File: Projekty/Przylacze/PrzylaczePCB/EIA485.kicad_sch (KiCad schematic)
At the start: 33 parts, among them Q10 BC557, Q11 BC547, Q12 BC547, Q9 2N7002, U4 MAX3485, U5 MAX3485

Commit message: Przyłącze - schemat elektryczny v1.1
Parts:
- D3, D5: footprint (none) -> 1_WLASNA_Library:2PAD_WIRE
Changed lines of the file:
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@@
       (effects (font (size 1.27 1.27)) (justify right))
     )
-    (property "Footprint" "" (at 130.81 130.81 0)
+    (property "Footprint" "1_WLASNA_Library:2PAD_WIRE" (at 130.81 130.81 0)
       (effects (font (size 1.27 1.27)) hide)
     )
@@
       (effects (font (size 1.27 1.27)) (justify right))
     )
-    (property "Footprint" "" (at 86.36 129.54 0)
-      (effects (font (size 1.27 1.27)) hide)
-    )
+    (property "Footprint" "1_WLASNA_Library:2PAD_WIRE" (at 86.36 129.54 0)
+      (effects (font (size 1.27 1.27)) hide)
+    )

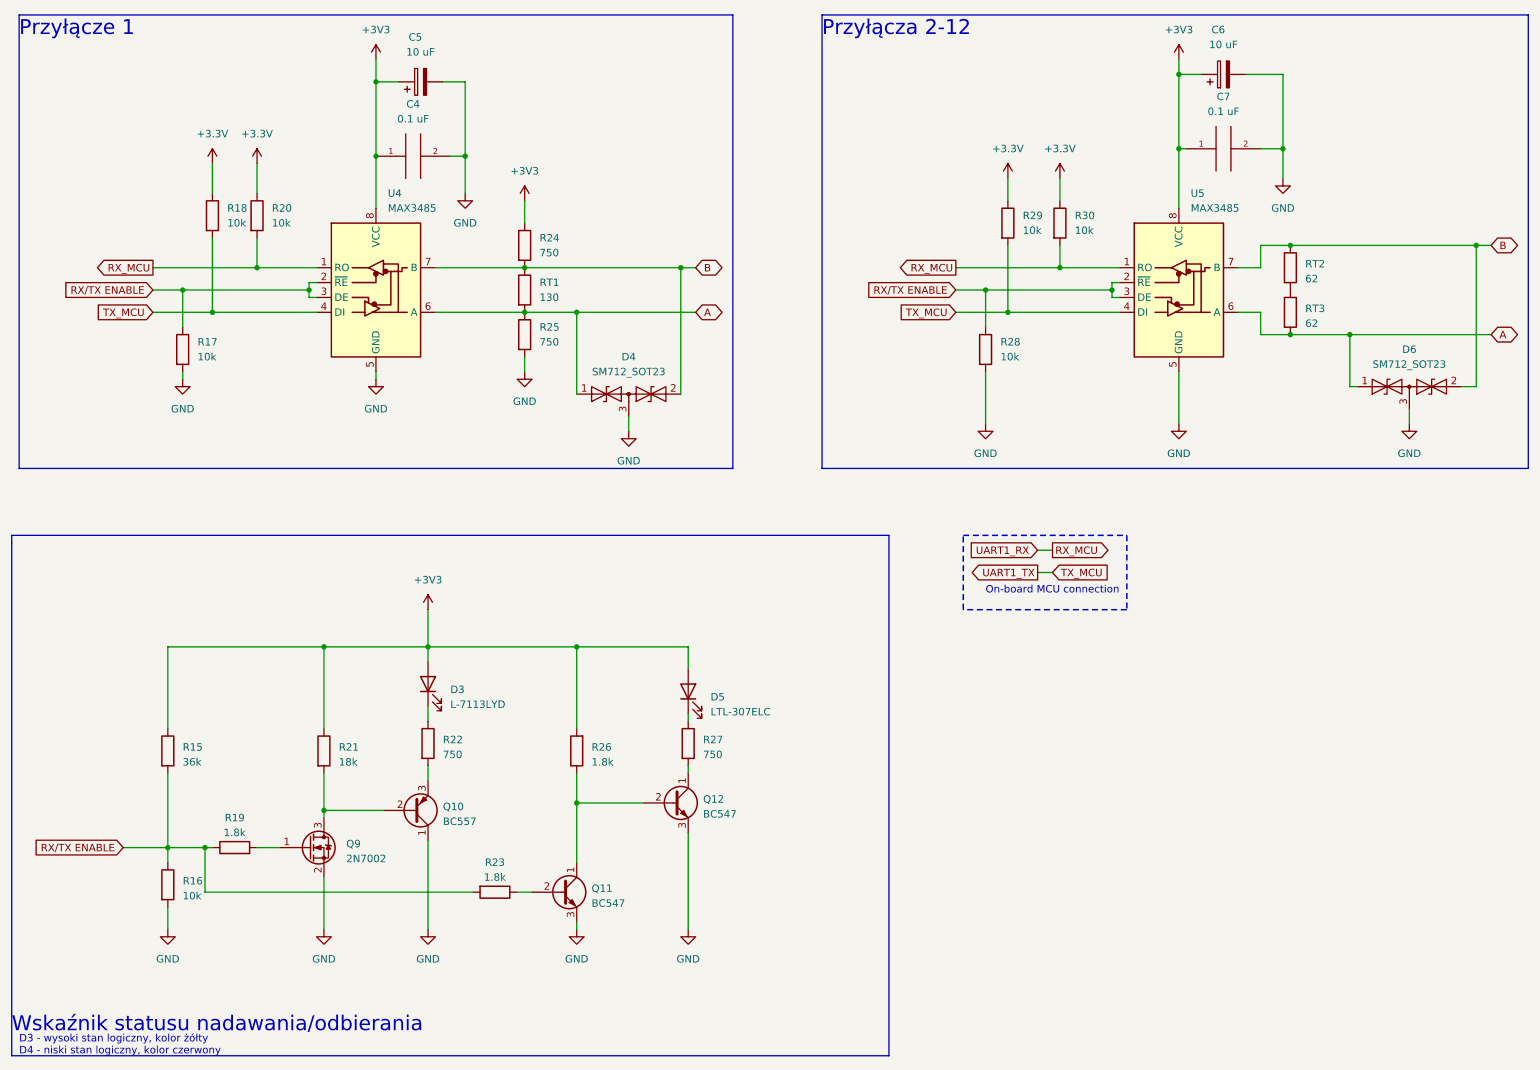
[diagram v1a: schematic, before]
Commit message: Połączenie w jeden schemat przyłącza sieci EIA485
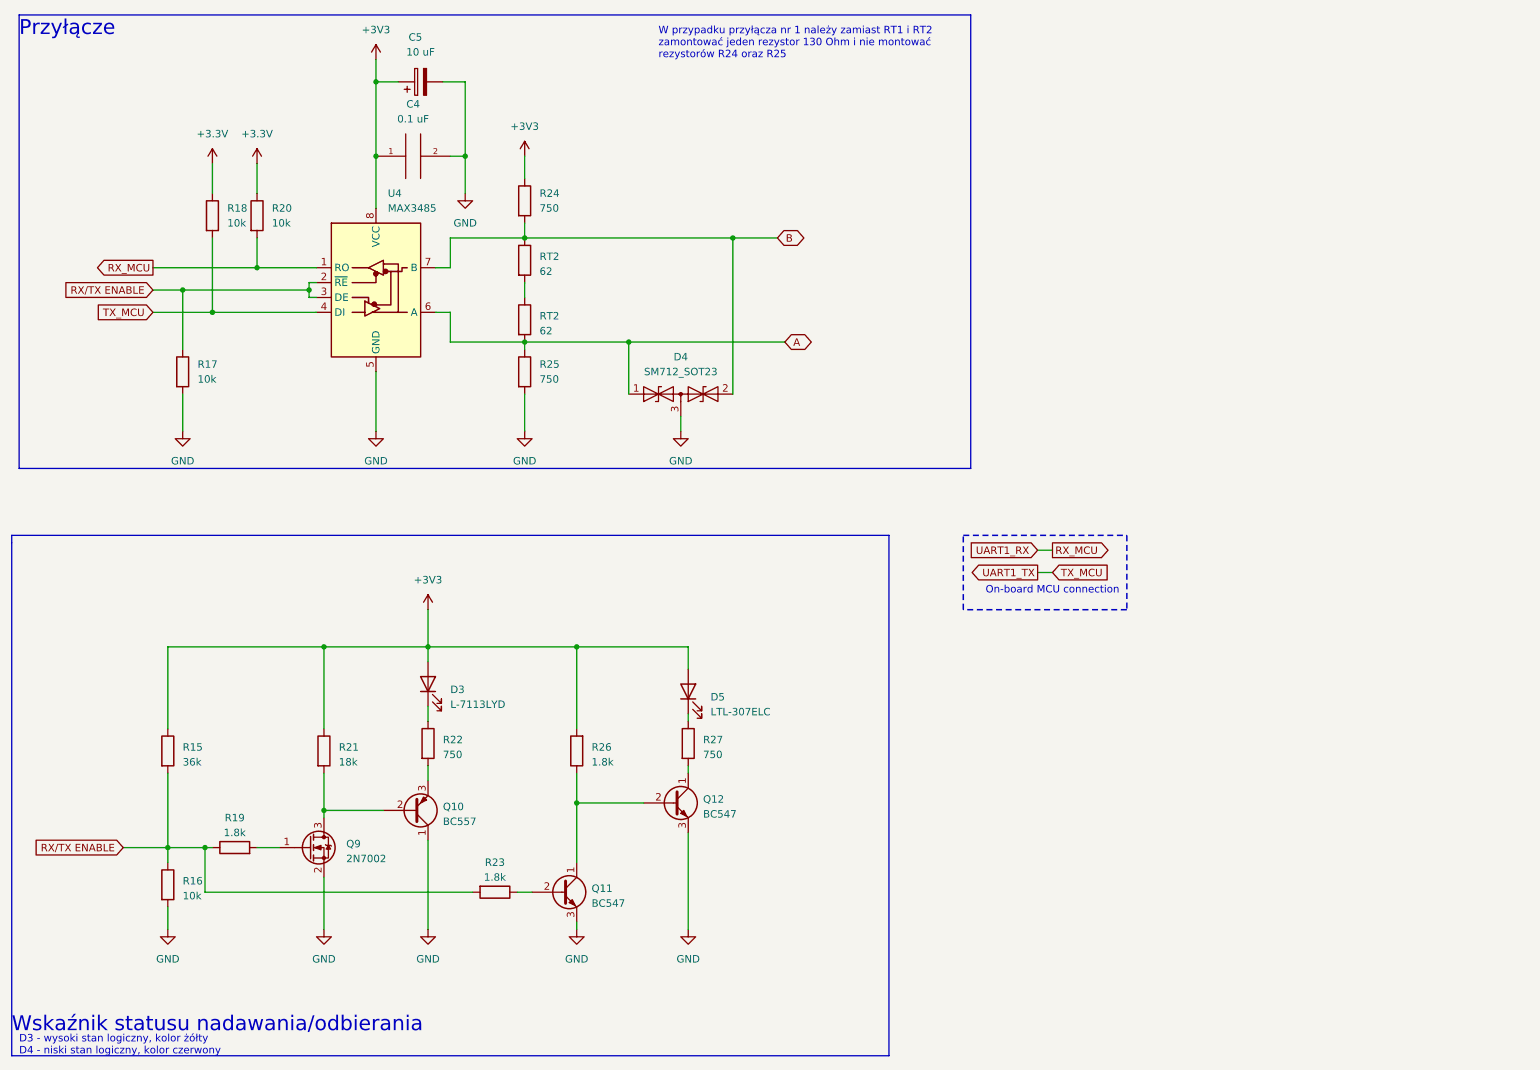
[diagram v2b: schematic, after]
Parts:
- removed C6: 10 uF, Capacitor_THT:CP_Radial_Tantal_D10.5mm_P5.00mm, symbol Device:C_Polarized
- removed C7: 0.1 uF, Capacitor_THT:C_Disc_D3.0mm_W1.6mm_P2.50mm, symbol pspice:C
- removed D6: SM712_SOT23, Package_TO_SOT_SMD:SOT-23, symbol Diode:SM712_SOT23
- removed R28, R29, R30: 10k, Resistor_THT:R_Axial_DIN0207_L6.3mm_D2.5mm_P7.62mm_Horizontal, symbol Device:R
- removed RT1: 130, Resistor_THT:R_Axial_DIN0207_L6.3mm_D2.5mm_P5.08mm_Vertical, symbol Device:R
- removed RT2, RT3: 62, Resistor_THT:R_Axial_DIN0207_L6.3mm_D2.5mm_P7.62mm_Horizontal, symbol Device:R
- removed U5: MAX3485, Package_SO:SO-8_3.9x4.9mm_P1.27mm, symbol Interface_UART:MAX3485
- added RT2 (x2): 62, Resistor_THT:R_Axial_DIN0207_L6.3mm_D2.5mm_P7.62mm_Horizontal, symbol Device:R
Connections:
- net A: now also RT2.2
- net B: now also RT2.1
- new net: RT2.1, RT2.2
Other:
- note added: "Przyłącze"
- note added: "W przypadku przyłącza nr 1 należy zamiast RT1 i RT2 zamontować jeden rezystor 130 Ohm i nie montować rezystorów R24 oraz R25"
- note removed: "Przyłącza 2-12"
- note removed: "Przyłącze 1"
- moved on the sheet: D4, R17, R24, R25

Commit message: Przyłącze - schemat elektryczny v1.2
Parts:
- C4: symbol pspice:C -> Device:C
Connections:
- net +3V3 renamed +3.3V
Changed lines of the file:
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@@
 (kicad_sch (version 20230121) (generator eeschema)
   (paper "A4")
+  (junction (at 66.04 62.23) (diameter 0) (color 0 0 0 0)
+  )
+  (junction (at 77.47 26.67) (diameter 0) (color 0 0 0 0)
+  )
+  (junction (at 111.76 149.86) (diameter 0) (color 0 0 0 0)
+  )
+  (junction (at 92.71 39.37) (diameter 0) (color 0 0 0 0)
+  )
+  (junction (at 102.87 71.12) (diameter 0) (color 0 0 0 0)
+  )
+  (junction (at 138.43 53.34) (diameter 0) (color 0 0 0 0)
+  )
+  (junction (at 68.58 123.19) (diameter 0) (color 0 0 0 0)
+  )
+  (junction (at 86.36 123.19) (diameter 0) (color 0 0 0 0)
+  )
+  (junction (at 120.65 71.12) (diameter 0) (color 0 0 0 0)
+  )
+  (junction (at 41.91 157.48) (diameter 0) (color 0 0 0 0)
+  )
+  (junction (at 57.15 58.42) (diameter 0) (color 0 0 0 0)
+  )
+  (junction (at 44.45 62.23) (diameter 0) (color 0 0 0 0)
+  )
+  (junction (at 68.58 151.13) (diameter 0) (color 0 0 0 0)
+  )
+  (junction (at 102.87 53.34) (diameter 0) (color 0 0 0 0)
+  )
+  (junction (at 49.53 66.04) (diameter 0) (color 0 0 0 0)
+  )
   (junction (at 77.47 39.37) (diameter 0) (color 0 0 0 0)
   )
-  (junction (at 66.04 62.23) (diameter 0) (color 0 0 0 0)
-  )
-  (junction (at 77.47 26.67) (diameter 0) (color 0 0 0 0)
-  )
-  (junction (at 111.76 149.86) (diameter 0) (color 0 0 0 0)
-  )
-  (junction (at 92.71 39.37) (diameter 0) (color 0 0 0 0)
-  )
-  (junction (at 102.87 71.12) (diameter 0) (color 0 0 0 0)
-  )
-  (junction (at 138.43 53.34) (diameter 0) (color 0 0 0 0)
-  )
-  (junction (at 68.58 123.19) (diameter 0) (color 0 0 0 0)
-  )
-  (junction (at 86.36 123.19) (diameter 0) (color 0 0 0 0)
-  )
-  (junction (at 120.65 71.12) (diameter 0) (color 0 0 0 0)
-  )
-  (junction (at 41.91 157.48) (diameter 0) (color 0 0 0 0)
-  )
-  (junction (at 57.15 58.42) (diameter 0) (color 0 0 0 0)
-  )
-  (junction (at 44.45 62.23) (diameter 0) (color 0 0 0 0)
-  )
-  (junction (at 68.58 151.13) (diameter 0) (color 0 0 0 0)
-  )
-  (junction (at 102.87 53.34) (diameter 0) (color 0 0 0 0)
-  )
-  (junction (at 49.53 66.04) (diameter 0) (color 0 0 0 0)
-  )
   (junction (at 111.76 123.19) (diameter 0) (color 0 0 0 0)
   )
@@
     (stroke (width 0) (type default))
   )
-  (wire (pts (xy 90.17 39.37) (xy 92.71 39.37))
+  (wire (pts (xy 87.63 39.37) (xy 92.71 39.37))
     (stroke (width 0) (type default))
   )
@@
   )
   (wire (pts (xy 57.15 40.64) (xy 57.15 45.72))
+    (stroke (width 0) (type default))
+  )
+  (wire (pts (xy 77.47 39.37) (xy 80.01 39.37))
     (stroke (width 0) (type default))
   )
@@
     )
   )
-  (symbol (lib_id "power:+3V3") (at 77.47 22.86 0) (unit 1)
-    (in_bom yes) (on_board yes) (dnp no) (fields_autoplaced)
-    (property "Reference" "#PWR024" (at 77.47 26.67 0)
-      (effects (font (size 1.27 1.27)) hide)
-    )
-    (property "Value" "+3V3" (at 77.47 17.78 0)
-      (effects (font (size 1.27 1.27)))
-    )
-    (property "Footprint" "" (at 77.47 22.86 0)
-      (effects (font (size 1.27 1.27)) hide)
-    )
-    (property "Datasheet" "" (at 77.47 22.86 0)
-      (effects (font (size 1.27 1.27)) hide)
-    )
-    (pin "1")
-    (instances
-      (project "PrzylaczePCB"
-        (path "/45db4533-aa6e-4785-aef0-204976ca4e66"
-          (reference "#PWR024") (unit 1)
-        )
-        (path "/45db4533-aa6e-4785-aef0-204976ca4e66/ce7112af-9253-43da-ac3f-57b598b98707"
-          (reference "#PWR027") (unit 1)
-        )
-      )
-      (project "rs485-przylacze"
-        (path "/84d4e166-b429-409a-ab37-c6a10fd82ff5"
-          (reference "#PWR?") (unit 1)
+  (symbol (lib_id "power:+3.3V") (at 86.36 116.84 0) (unit 1)
+    (in_bom yes) (on_board yes) (dnp no)
+    (property "Reference" "#PWR014" (at 86.36 120.65 0)
+      (effects (font (size 1.27 1.27)) hide)
+    )
+    (property "Value" "+3.3V" (at 86.36 113.03 0)
+      (effects (font (size 1.27 1.27)))
+    )
+    (property "Footprint" "" (at 86.36 116.84 0)
+      (effects (font (size 1.27 1.27)) hide)
+    )
+    (property "Datasheet" "" (at 86.36 116.84 0)
+      (effects (font (size 1.27 1.27)) hide)
+    )
+    (pin "1")
+    (instances
+      (project "PrzylaczePCB"
+        (path "/45db4533-aa6e-4785-aef0-204976ca4e66"
+          (reference "#PWR014") (unit 1)
+        )
+        (path "/45db4533-aa6e-4785-aef0-204976ca4e66/ce7112af-9253-43da-ac3f-57b598b98707"
+          (reference "#PWR019") (unit 1)
         )
       )
@@
     )
   )
-  (symbol (lib_id "pspice:C") (at 83.82 39.37 90) (unit 1)
+  (symbol (lib_id "Device:C") (at 83.82 39.37 90) (unit 1)
     (in_bom yes) (on_board yes) (dnp no) (fields_autoplaced)
     (property "Reference" "C4" (at 83.82 30.48 90)
@@
       (effects (font (size 1.27 1.27)))
     )
-    (property "Footprint" "Capacitor_THT:C_Disc_D3.0mm_W1.6mm_P2.50mm" (at 83.82 39.37 0)
+    (property "Footprint" "Capacitor_THT:C_Disc_D3.0mm_W1.6mm_P2.50mm" (at 87.63 38.4048 0)
       (effects (font (size 1.27 1.27)) hide)
     )
@@
     )
   )
+  (symbol (lib_id "power:+3.3V") (at 102.87 39.37 0) (unit 1)
+    (in_bom yes) (on_board yes) (dnp no)
+    (property "Reference" "#PWR014" (at 102.87 43.18 0)
+      (effects (font (size 1.27 1.27)) hide)
+    )
+    (property "Value" "+3.3V" (at 102.87 35.56 0)
+      (effects (font (size 1.27 1.27)))
+    )
+    (property "Footprint" "" (at 102.87 39.37 0)
+      (effects (font (size 1.27 1.27)) hide)
+    )
+    (property "Datasheet" "" (at 102.87 39.37 0)
+      (effects (font (size 1.27 1.27)) hide)
+    )
+    (pin "1")
+    (instances
+      (project "PrzylaczePCB"
+        (path "/45db4533-aa6e-4785-aef0-204976ca4e66"
+          (reference "#PWR014") (unit 1)
+        )
+        (path "/45db4533-aa6e-4785-aef0-204976ca4e66/ce7112af-9253-43da-ac3f-57b598b98707"
+          (reference "#PWR011") (unit 1)
+        )
+      )
+    )
+  )
   (symbol (lib_id "power:GND") (at 77.47 86.36 0) (unit 1)
     (in_bom yes) (on_board yes) (dnp no) (fields_autoplaced)
@@
     )
   )
-  (symbol (lib_id "power:+3V3") (at 86.36 116.84 0) (unit 1)
-    (in_bom yes) (on_board yes) (dnp no) (fields_autoplaced)
-    (property "Reference" "#PWR026" (at 86.36 120.65 0)
-      (effects (font (size 1.27 1.27)) hide)
-    )
-    (property "Value" "+3V3" (at 86.36 111.76 0)
-      (effects (font (size 1.27 1.27)))
-    )
-    (property "Footprint" "" (at 86.36 116.84 0)
-      (effects (font (size 1.27 1.27)) hide)
-    )
-    (property "Datasheet" "" (at 86.36 116.84 0)
-      (effects (font (size 1.27 1.27)) hide)
-    )
-    (pin "1")
-    (instances
-      (project "PrzylaczePCB"
-        (path "/45db4533-aa6e-4785-aef0-204976ca4e66"
-          (reference "#PWR026") (unit 1)
-        )
-        (path "/45db4533-aa6e-4785-aef0-204976ca4e66/ce7112af-9253-43da-ac3f-57b598b98707"
-          (reference "#PWR029") (unit 1)
-        )
-      )
-      (project "rs485-przylacze"
-        (path "/84d4e166-b429-409a-ab37-c6a10fd82ff5"
-          (reference "#PWR07") (unit 1)
+  (symbol (lib_id "power:+3.3V") (at 77.47 22.86 0) (unit 1)
+    (in_bom yes) (on_board yes) (dnp no)
+    (property "Reference" "#PWR014" (at 77.47 26.67 0)
+      (effects (font (size 1.27 1.27)) hide)
+    )
+    (property "Value" "+3.3V" (at 77.47 19.05 0)
+      (effects (font (size 1.27 1.27)))
+    )
+    (property "Footprint" "" (at 77.47 22.86 0)
+      (effects (font (size 1.27 1.27)) hide)
+    )
+    (property "Datasheet" "" (at 77.47 22.86 0)
+      (effects (font (size 1.27 1.27)) hide)
+    )
+    (pin "1")
+    (instances
+      (project "PrzylaczePCB"
+        (path "/45db4533-aa6e-4785-aef0-204976ca4e66"
+          (reference "#PWR014") (unit 1)
+        )
+        (path "/45db4533-aa6e-4785-aef0-204976ca4e66/ce7112af-9253-43da-ac3f-57b598b98707"
+          (reference "#PWR09") (unit 1)
         )
       )
@@
         )
       )
-    )
-  )
-  (symbol (lib_id "power:+3V3") (at 102.87 39.37 0) (unit 1)
-    (in_bom yes) (on_board yes) (dnp no) (fields_autoplaced)
-    (property "Reference" "#PWR029" (at 102.87 43.18 0)
-      (effects (font (size 1.27 1.27)) hide)
-    )
-    (property "Value" "+3V3" (at 102.87 34.29 0)
-      (effects (font (size 1.27 1.27)))
-    )
-    (property "Footprint" "" (at 102.87 39.37 0)
-      (effects (font (size 1.27 1.27)) hide)
-    )
-    (property "Datasheet" "" (at 102.87 39.37 0)
-      (effects (font (size 1.27 1.27)) hide)
-    )
-    (pin "1")
-    (instances
-      (project "PrzylaczePCB"
-        (path "/45db4533-aa6e-4785-aef0-204976ca4e66"
-          (reference "#PWR029") (unit 1)
-        )
-        (path "/45db4533-aa6e-4785-aef0-204976ca4e66/ce7112af-9253-43da-ac3f-57b598b98707"
-          (reference "#PWR032") (unit 1)
-        )
-      )
-      (project "rs485-przylacze"
-        (path "/84d4e166-b429-409a-ab37-c6a10fd82ff5"
-          (reference "#PWR?") (unit 1)
-        )
-      )

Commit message: Przyłącze - projekt PCB v0.2
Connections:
- net RX/TX ENABLE  is gone; now on net RX/TX ENABLE: R15.2, R16.1, R19.1, R23.2
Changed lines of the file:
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@@
     )
   )
-  (global_label "RX{slash}TX ENABLE " (shape input) (at 34.29 157.48 180) (fields_autoplaced)
+  (global_label "RX{slash}TX ENABLE" (shape input) (at 34.29 157.48 180) (fields_autoplaced)
     (effects (font (size 1.27 1.27)) (justify right))
-    (property "Intersheetrefs" "${INTERSHEET_REFS}" (at 16.4467 157.48 0)
+    (property "Intersheetrefs" "${INTERSHEET_REFS}" (at 17.4143 157.48 0)
       (effects (font (size 1.27 1.27)) (justify right) hide)
     )
